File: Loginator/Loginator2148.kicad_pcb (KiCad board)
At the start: 2 copper layers, 61 x 38.1 mm, 66 parts, among them J001 USB_MICROB, J002 M01PTH, J301 JST 2mm, J401 M06, J402 M04, J403 M10, J404 M06, J406 11DoF, J701 Micro_SD_Card_Det_Hirose_DM3AT, Q050 PMOS, Q201 PMOS, U201 MIC5319, U202 MAX4173, U301 MCP73831, U401 LPC2148, U402 1525, Y401 12MHz

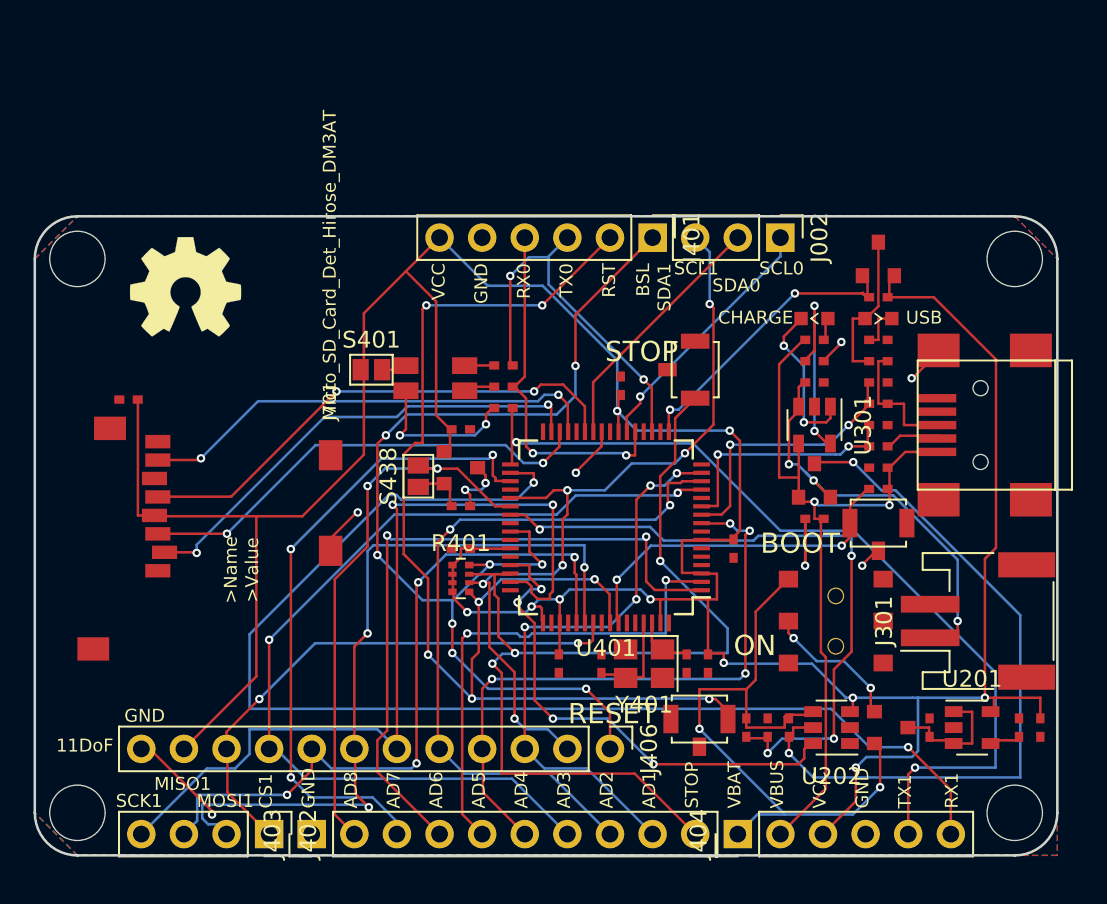
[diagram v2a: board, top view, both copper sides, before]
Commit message: Fixed backwards pin issue on current sensor, combined some resistors into arrays, fixed inherited error in USB resistors
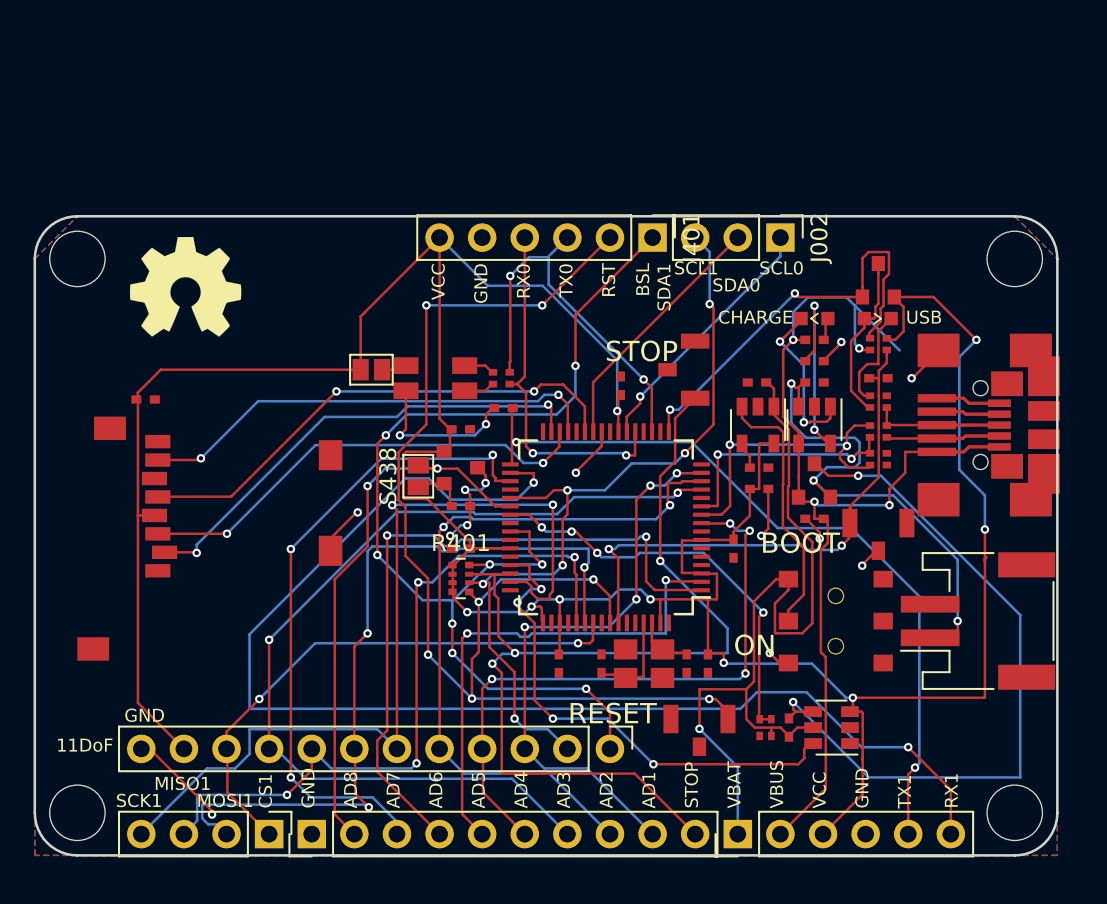
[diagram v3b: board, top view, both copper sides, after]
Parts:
- removed C020, C030: 18pF, KwanSystems:SMD_0402
- removed Q201: PMOS, KwanSystems:SOT-23
- removed R010, R051: 10k, KwanSystems:SMD_0402
- removed R020, R030, R421: 33, KwanSystems:SMD_0402
- removed R031, R050: 1.5k, KwanSystems:SMD_0402
- removed R202: 100k, KwanSystems:SMD_0402
- removed U$1: , KWAN_CIRCLE
- added C023: 18pF, KwanSystems:R_Array_Convex_2x0402, F.Cu at (50.3, -23.6)
- added G***: LOGO, KwanSystems:KWAN_CIRCLE_soldermask, B.Cu at (4.57, -28.4)
- added R015: 10k, KwanSystems:R_Array_Convex_2x0402, F.Cu at (50.3, -30.5)
- added R023: 33, KwanSystems:R_Array_Convex_2x0402, F.Cu at (50.3, -25.3)
- added R035: 1.5k, KwanSystems:R_Array_Convex_2x0402, F.Cu at (50.3, -27.1)
- J001: footprint KwanSystems:USB_Mini-B -> USB_Double-B
- R011: value 100k -> 22k
- R201, R419: footprint KwanSystems:SMD_0402 -> KwanSystems:R_Array_Convex_2x0402
- moved C204 23.0 mm to (43.1, -28.2), turned to 180 degrees
- moved U201 22.1 mm to (43.1, -25.7), turned to 270 degrees
- moved C201 22.0 mm to (43.2, -21.8), turned to 0 degrees
- moved C203 21.9 mm to (43.2, -23.1), turned to 0 degrees
- moved R011 5.33 mm to (50.3, -28.4), turned to 180 degrees
- moved Q050 1.27 mm to (50.3, -34.3)
- moved R201 1.14 mm to (43.6, -7.62), turned to 90 degrees
- moved C701 1.02 mm to (6.60, -27.2), turned to 0 degrees
- moved R419 0.77 mm to (27.8, -28.4), turned to 0 degrees
- turned R203 to 270 degrees
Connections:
- net /N$1 renamed /C_LED+
- net /N$17 renamed /BYP
- net /N$2 renamed /PROG
- net /N$3 renamed /C+LED-
- net /N$6 renamed /UC_LED+
- C204 pad 1: /RAW -> /VIN-
- D050 pad 1: /N$7 -> /UC_LED-
- R011 pad 2: /VBUS -> /USB_ON
- R201 pad 1: /VIN- -> GND
- R201 pad 2: /BATLVL -> /VIN-
- R419 pad 1: /TX0(PWMB) -> /DB
- R419 pad 2: /DB -> /DG
- S201 pad 2: /N$10 -> /PWR_EN
- U201 pad 1: /RAW -> /VIN-
- U201 pad 3: /RAW -> /PWR_EN
- U202 pad 4: /VIN- -> /VIN+
- U202 pad 5: /VIN+ -> /VIN-
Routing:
- net /PWR_EN: track 0.00 -> 15.7 mm
- net /BATLVL: track 40.2 -> 24.9 mm
- net /VBUS: track 46.9 -> 60.8 mm, vias 2 -> 4
- net /USB_ON: track 20.8 -> 33.1 mm
- net /VIN-: track 39.4 -> 49.1 mm, vias 2 -> 1
- net /N$10: track 8.48 -> 0.00 mm, vias 2 -> 0
- net /USB_SOFTCONNECT: track 18.0 -> 26.0 mm
- net /RAW: track 7.75 -> 0.00 mm
- net /TX1(PWMR): track 52.6 -> 46.0 mm
- net /UC_LED-: track 0.00 -> 6.26 mm
- net /VLIPO: track 25.4 -> 31.3 mm
- net VCC: track 204.7 -> 199.1 mm, vias 10 -> 9
- net GND: track 26.2 -> 29.8 mm, vias 9 -> 13
- net Net-(J001-Pad4): track 0.00 -> 2.98 mm
- net /CONN_D-: track 3.37 -> 6.17 mm
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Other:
- board text added: "01 Sep 2017"
- board text added: "Loginator v2.0"
- board text added: "https://stkwans.blogspot.com https://github.com/kwan3217"
- board text removed: "13 Apr 2012"
- board text removed: "Loginator v1.1"
- board text removed: "stkwans.blogspot.com"

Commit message: More work on Loginator
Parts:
- removed C203: 100nF, KwanSystems:SMD_0402
- added C205: 4.7nF, KwanSystems:SMD_0402, F.Cu at (43.2, -21.8)
- C201: value 4.7nF -> 1uF
- C204: value 1uF -> 100nF
- U201: value MIC5319 -> 3.3V
- moved C201 6.35 mm to (43.1, -28.2), turned to 180 degrees
- moved C204 5.08 mm to (43.2, -23.1), turned to 0 degrees
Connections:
- net /PWR_EN renamed /Sheet59FCEA5F/PWR_EN
- C201 pad 1: VCC -> /VIN-
- C204 pad 1: /VIN- -> /Sheet59FCEA5F/BYP
- J701 pad 1: Net-(J701-Pad1) -> (no net)
- J701 pad 10: Net-(J701-Pad10) -> (no net)
- J701 pad 11: GND -> (no net)
- J701 pad 12: GND -> (no net)
- J701 pad 8: Net-(J701-Pad8) -> (no net)
- S201 pad 1: GND -> /VIN-
- S201 pad 3: /VIN- -> GND
- U201 pad 4: /BYP -> /Sheet59FCEA5F/BYP
- U401 pad 12: Net-(U401-Pad12) -> (no net)
- U401 pad 16: Net-(U401-Pad16) -> (no net)
- U401 pad 20: Net-(U401-Pad20) -> (no net)
- U401 pad 24: Net-(U401-Pad24) -> (no net)
- U401 pad 28: Net-(U401-Pad28) -> (no net)
- U401 pad 32: Net-(U401-Pad32) -> (no net)
- U401 pad 36: Net-(U401-Pad36) -> (no net)
- U401 pad 4: Net-(U401-Pad4) -> (no net)
- U401 pad 40: Net-(U401-Pad40) -> (no net)
- U401 pad 44: Net-(U401-Pad44) -> (no net)
- U401 pad 48: Net-(U401-Pad48) -> (no net)
- U401 pad 5: Net-(U401-Pad5) -> (no net)
- U401 pad 52: Net-(U401-Pad52) -> (no net)
- U401 pad 56: Net-(U401-Pad56) -> (no net)
- U401 pad 60: Net-(U401-Pad60) -> (no net)
- U401 pad 64: Net-(U401-Pad64) -> (no net)
- U401 pad 8: Net-(U401-Pad8) -> (no net)
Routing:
- net /VBUS: track 60.8 -> 57.3 mm
- net /Sheet59FCEA5F/BYP: track 0.00 -> 1.63 mm
- net /BYP: track 1.63 -> 0.00 mm
- net GND: track 29.8 -> 28.5 mm, vias 13 -> 12

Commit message: Starting IOIO_Sensinator
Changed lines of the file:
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@@
     (pad 5 connect rect (at 7 1.6 180) (size 1.524 0.2) (layers Top)
       (net 2 GND))
-    (pad 1 connect roundrect (at 6.1 -1.45 225) (size 0.6242 0.2) (layers Top)(roundrect_rratio 0.5)
+    (pad 1 connect rect (at 6.1 -1.45 225) (size 0.6242 0.2) (layers Top)
       (net 6 /VBUS))
-    (pad 5 connect roundrect (at 6.1 1.45 135) (size 0.6242 0.2) (layers Top)(roundrect_rratio 0.5)
+    (pad 5 connect rect (at 6.1 1.45 135) (size 0.6242 0.2) (layers Top)
       (net 2 GND))
-    (pad 2 connect roundrect (at 6.225 -0.725 225) (size 0.4121 0.2) (layers Top)(roundrect_rratio 0.5)
+    (pad 2 connect rect (at 6.225 -0.725 225) (size 0.4121 0.2) (layers Top)
       (net 34 /CONN_D-))
-    (pad 4 connect roundrect (at 6.225 0.725 135) (size 0.4121 0.2) (layers Top)(roundrect_rratio 0.5)
+    (pad 4 connect rect (at 6.225 0.725 135) (size 0.4121 0.2) (layers Top)
       (net 48 "Net-(J001-Pad4)"))
     (model ../KwanSystems.pretty/Molex_47346_0001.wrl
